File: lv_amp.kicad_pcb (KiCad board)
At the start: 2 copper layers, 127 x 76.2 mm, 87 parts, among them J1 Jack-DC, J2 AudioJack2, J3 AudioJack2, Q1 Q_NMOS_DGS, U1 MAX1771xSA, U2 TL072, U3 ECC83, U4 ECC83, U5 ECC83

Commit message: alpha1 complete
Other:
- board text added: "lv-amp alpha1"
- board text removed: "lv-amp alpha0"
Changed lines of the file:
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@@
   (gr_line (start 38.1 63.5) (end 38.1 139.7) (layer "Edge.Cuts") (width 0.1))
   (gr_line (start 165.1 139.7) (end 165.1 63.5) (layer "Edge.Cuts") (width 0.1))
-  (gr_text "lv-amp alpha0" (at 140 80) (layer "B.SilkS")
+  (gr_text "lv-amp alpha1" (at 140 80) (layer "B.SilkS")
     (effects (font (size 1 1) (thickness 0.15)) (justify mirror))
   )

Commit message: shuffle stuff around to minimize antenna length
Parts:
- moved C6 11.9 mm to (129.0, 92.2), turned to 0 degrees
- moved C4 6.82 mm to (118.5, 97.2), turned to -90 degrees
- moved R7 4.37 mm to (120.0, 89.2), turned to -90 degrees
- moved C5 3.18 mm to (113.5, 87.5)
- moved C7 2.38 mm to (122.8, 98.5), turned to 0 degrees
- moved R11 2.36 mm to (135.0, 91.8), turned to -90 degrees
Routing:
- net +12V: track 223.4 -> 232.8 mm
- net /u1ap: track 31.1 -> 32.8 mm, vias 0 -> 1
- net /q1s: track 15.3 -> 16.6 mm
- net Net-(R7-Pad1): track 7.02 -> 5.81 mm
- net HT: track 201.4 -> 200.3 mm
- net GND: vias 11 -> 12

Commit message: 5v zener
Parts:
- D2: value Zener 3.3V -> Zener 5V
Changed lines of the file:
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@@
   (net 35 "Net-(R7-Pad1)")
   (net 36 "Net-(R6-Pad1)")
-  (net 37 "Net-(R21-Pad2)")
+  (net 37 "Net-(C24-Pad1)")
   (net 38 "/u3ag")
   (net 39 "Net-(R24-Pad1)")
@@
       (effects (font (size 1 1) (thickness 0.15)))
     )
-    (fp_text value "Zener 3.3V" (at 0 2.5) (layer "F.Fab")
+    (fp_text value "Zener 5V" (at 0 2.5) (layer "F.Fab")
       (effects (font (size 1 1) (thickness 0.15)))
     )
@@
     (pad "" smd rect locked (at -1 0.95 180) (size 0.9 0.8) (layers "F.Cu" "F.Paste" "F.Mask"))
     (pad "1" smd rect locked (at 1 0 180) (size 0.9 0.8) (layers "F.Cu" "F.Paste" "F.Mask")
-      (net 37 "Net-(R21-Pad2)") (pinfunction "K") (pintype "passive"))
+      (net 37 "Net-(C24-Pad1)") (pinfunction "K") (pintype "passive"))
     (pad "2" smd rect locked (at -1 -0.95 180) (size 0.9 0.8) (layers "F.Cu" "F.Paste" "F.Mask")
       (net 9 "GND") (pinfunction "A") (pintype "passive"))
@@
     (fp_circle (center 0 0) (end 2 0) (layer "F.Fab") (width 0.1) (fill none))
     (pad "1" smd roundrect locked (at -1.8 0) (size 2.6 1.6) (layers "F.Cu" "F.Paste" "F.Mask") (roundrect_rratio 0.15625)
-      (net 37 "Net-(R21-Pad2)") (pintype "passive"))
+      (net 37 "Net-(C24-Pad1)") (pintype "passive"))
     (pad "2" smd roundrect locked (at 1.8 0) (size 2.6 1.6) (layers "F.Cu" "F.Paste" "F.Mask") (roundrect_rratio 0.15625)
       (net 9 "GND") (pintype "passive"))
@@
       (net 9 "GND") (pinfunction "V-") (pintype "power_in"))
     (pad "5" smd roundrect locked (at 2.575 1.905 90) (size 1.75 0.6) (layers "F.Cu" "F.Paste" "F.Mask") (roundrect_rratio 0.25)
-      (net 37 "Net-(R21-Pad2)") (pinfunction "+") (pintype "input"))
+      (net 37 "Net-(C24-Pad1)") (pinfunction "+") (pintype "input"))
     (pad "6" smd roundrect locked (at 2.575 0.635 90) (size 1.75 0.6) (layers "F.Cu" "F.Paste" "F.Mask") (roundrect_rratio 0.25)
       (net 49 "Net-(U2-Pad3)") (pinfunction "-") (pintype "input"))
@@
       (net 17 "+12V") (pintype "passive"))
     (pad "2" smd roundrect locked (at 0.825 0) (size 0.8 0.95) (layers "F.Cu" "F.Paste" "F.Mask") (roundrect_rratio 0.25)
-      (net 37 "Net-(R21-Pad2)") (pintype "passive"))
+      (net 37 "Net-(C24-Pad1)") (pintype "passive"))
     (model "${KICAD6_3DMODEL_DIR}/Resistor_SMD.3dshapes/R_0603_1608Metric.wrl"
       (offset (xyz 0 0 0))

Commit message: use 5.1 zener
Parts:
- D2: value Zener 5V -> Zener 5.1V
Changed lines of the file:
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@@
       (effects (font (size 1 1) (thickness 0.15)))
     )
-    (fp_text value "Zener 5V" (at 0 2.5) (layer "F.Fab")
+    (fp_text value "Zener 5.1V" (at 0 2.5) (layer "F.Fab")
       (effects (font (size 1 1) (thickness 0.15)))
     )

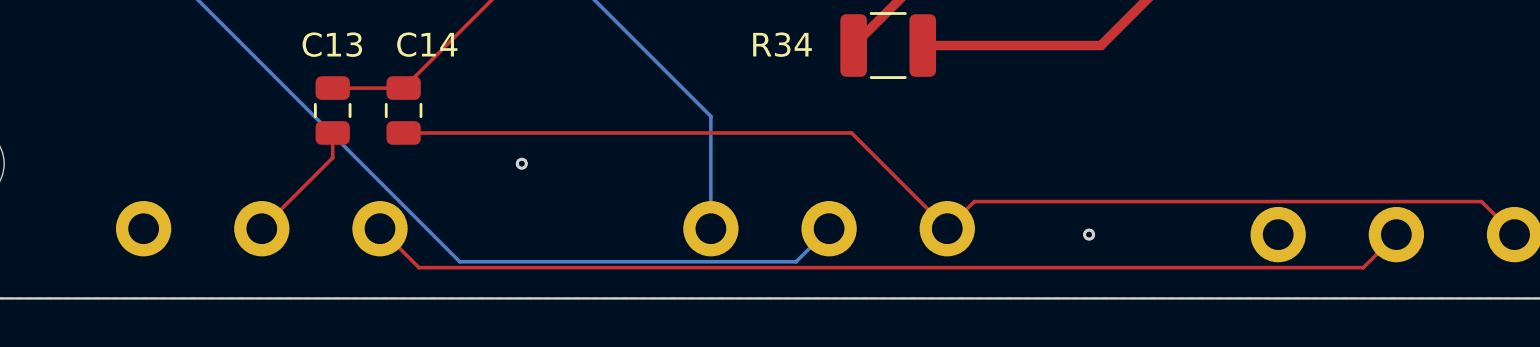
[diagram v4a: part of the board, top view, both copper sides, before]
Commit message: Oops un-flip mid pot
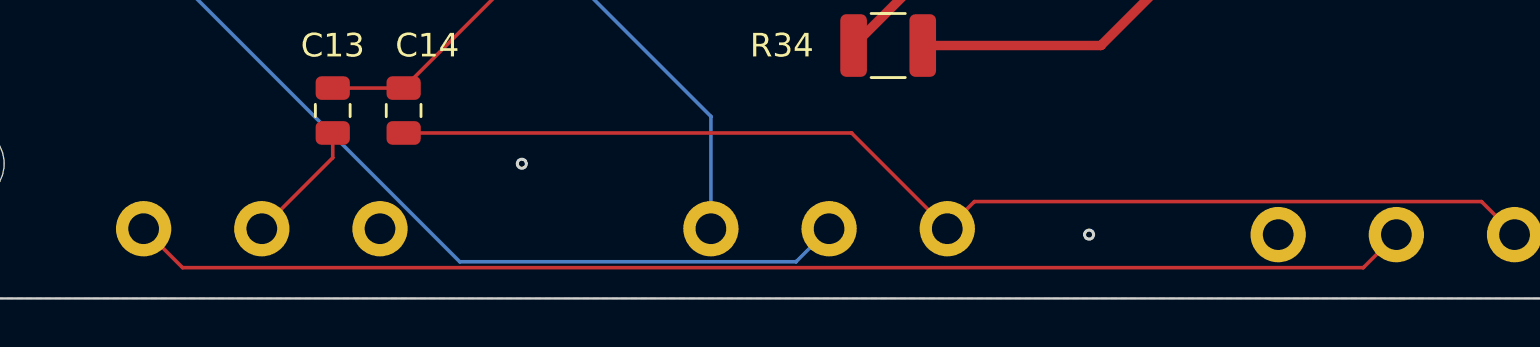
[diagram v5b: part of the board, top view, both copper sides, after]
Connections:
- RV4 pad 1: Net-(RV2-Pad2) -> GND
- RV4 pad 3: GND -> Net-(RV2-Pad2)
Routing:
- net Net-(RV2-Pad2): track 44.3 -> 54.3 mm
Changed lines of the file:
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@@
     (property "Sheetfile" "lv_amp.kicad_sch")
     (property "Sheetname" "")
-    (property "Source" "https://www.tubesandmore.com/products/socket-9-pin-ceramic-pc-mount-bottom-or-pc-mount")
+    (property "Vendor" "https://www.tubesandmore.com/products/socket-9-pin-ceramic-pc-mount-bottom-or-pc-mount")
     (fp_text reference "U3" (at 4 15) (layer "B.SilkS")
       (effects (font (size 1 1) (thickness 0.15)) (justify mirror))
@@
     (property "Sheetfile" "lv_amp.kicad_sch")
     (property "Sheetname" "")
-    (property "source" "https://www.tubesandmore.com/products/potentiometer-alpha-audio-solid-shaft-pc-lead-16mm")
+    (property "Vendor" "https://www.tubesandmore.com/products/potentiometer-alpha-audio-solid-shaft-pc-lead-16mm")
     (attr through_hole)
     (fp_text reference "RV2" (at -5 -1 180) (layer "B.SilkS")
@@
     (property "Sheetfile" "lv_amp.kicad_sch")
     (property "Sheetname" "")
-    (property "Source" "https://www.tubesandmore.com/products/potentiometer-alpha-audio-solid-shaft-pc-lead-16mm")
+    (property "Vendor" "https://www.tubesandmore.com/products/potentiometer-alpha-linear-solid-shaft-pc-lead-16mm")
     (attr through_hole)
     (fp_text reference "RV4" (at -4.75 0 180) (layer "B.SilkS")
@@
     (fp_line (start 1.5 1.5) (end 6.5 1.5) (layer "B.Fab") (width 0.1))
     (pad "1" thru_hole circle locked (at 0 0 270) (size 2.34 2.34) (drill 1.3) (layers *.Cu *.Mask)
-      (net 48 "Net-(RV2-Pad2)") (pinfunction "1") (pintype "passive"))
+      (net 9 "GND") (pinfunction "1") (pintype "passive"))
     (pad "2" thru_hole circle locked (at 0 5 270) (size 2.34 2.34) (drill 1.3) (layers *.Cu *.Mask)
       (net 11 "Net-(C13-Pad2)") (pinfunction "2") (pintype "passive"))
     (pad "3" thru_hole circle locked (at 0 10 270) (size 2.34 2.34) (drill 1.3) (layers *.Cu *.Mask)
-      (net 9 "GND") (pinfunction "3") (pintype "passive"))
+      (net 48 "Net-(RV2-Pad2)") (pinfunction "3") (pintype "passive"))
     (model "${KICAD6_3DMODEL_DIR}/Potentiometer_THT.3dshapes/Potentiometer_Piher_T-16H_Single_Horizontal.wrl"
       (offset (xyz 0 0 0))
@@
     (property "Sheetfile" "lv_amp.kicad_sch")
     (property "Sheetname" "")
+    (property "Vendor" "https://www.tubesandmore.com/products/socket-9-pin-ceramic-pc-mount-bottom-or-pc-mount")
     (fp_text reference "U5" (at -7.1 12.7) (layer "B.SilkS")
       (effects (font (size 1 1) (thickness 0.15)) (justify mirror))
@@
     (property "Sheetfile" "lv_amp.kicad_sch")
     (property "Sheetname" "")
-    (property "Source" "https://www.tubesandmore.com/products/potentiometer-alpha-audio-solid-shaft-pc-lead-16mm")
+    (property "Vendor" "https://www.tubesandmore.com/products/potentiometer-alpha-audio-solid-shaft-pc-lead-16mm")
     (attr through_hole)
     (fp_text reference "RV1" (at -4.75 -1 180) (layer "B.SilkS")
@@
     (property "Sheetfile" "lv_amp.kicad_sch")
     (property "Sheetname" "")
-    (property "Source" "https://www.tubesandmore.com/products/potentiometer-alpha-audio-solid-shaft-pc-lead-16mm")
+    (property "Vendor" "https://www.tubesandmore.com/products/potentiometer-alpha-linear-solid-shaft-pc-lead-16mm")
     (attr through_hole)
     (fp_text reference "RV3" (at -4.75 -1 180) (layer "B.SilkS")
@@
     (property "Sheetfile" "lv_amp.kicad_sch")
     (property "Sheetname" "")
+    (property "Vendor" "https://www.tubesandmore.com/products/potentiometer-alpha-audio-solid-shaft-pc-lead-16mm")
     (attr exclude_from_pos_files)
     (fp_text reference "TP1" (at 0 3) (layer "B.SilkS")
@@
   (segment (start 76.420396 74) (end 71.909831 69.489435) (width 0.4) (layer "F.Cu") (net 46))
   (segment (start 76.9625 74) (end 76.420396 74) (width 0.4) (layer "F.Cu") (net 46))
-  (segment (start 101.601889 138.398111) (end 61.648111 138.398111) (width 0.1524) (layer "F.Cu") (net 48))
-  (segment (start 61.648111 138.398111) (end 60 136.75) (width 0.1524) (layer "F.Cu") (net 48))
-  (segment (start 103 137) (end 101.601889 138.398111) (width 0.1524) (layer "F.Cu") (net 48))
+  (segment (start 50 136.75) (end 51.648111 138.398111) (width 0.1524) (layer "F.Cu") (net 48))
+  (segment (start 101.601889 138.398111) (end 103 137) (width 0.1524) (layer "F.Cu") (net 48))
+  (segment (start 51.648111 138.398111) (end 101.601889 138.398111) (width 0.1524) (layer "F.Cu") (net 48))
   (segment (start 49.765 116.305) (end 49.765 121.455) (width 0.1524) (layer "F.Cu") (net 49))
   (segment (start 48.495 116.305) (end 49.765 116.305) (width 0.1524) (layer "F.Cu") (net 49))

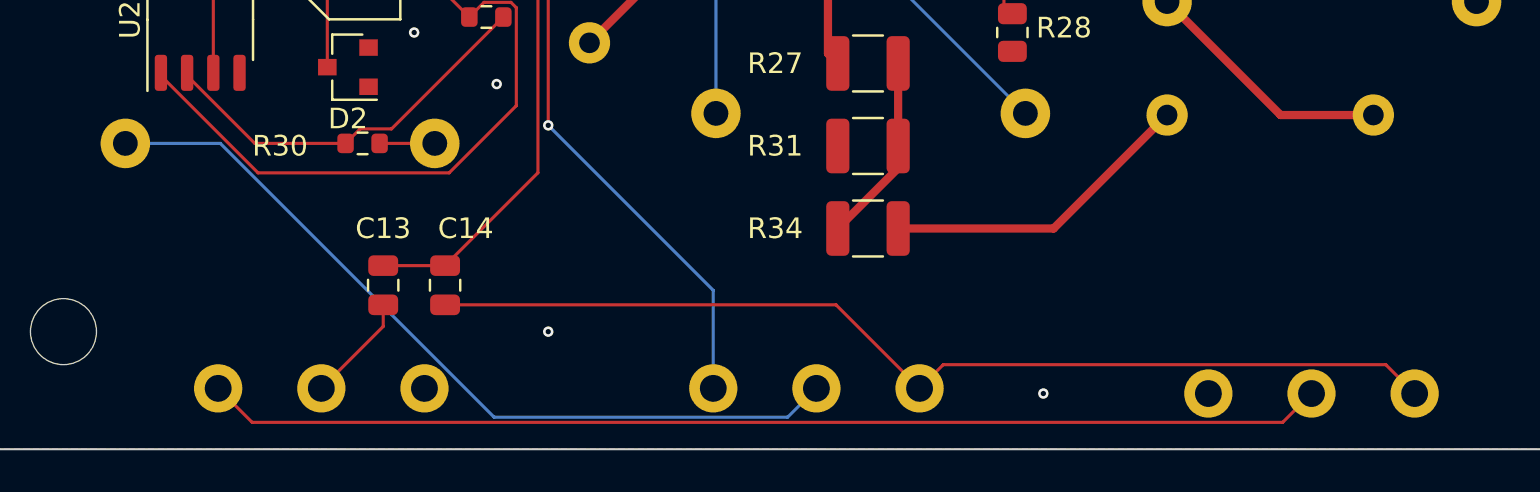
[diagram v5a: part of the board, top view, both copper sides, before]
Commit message: Errata: flip pot order
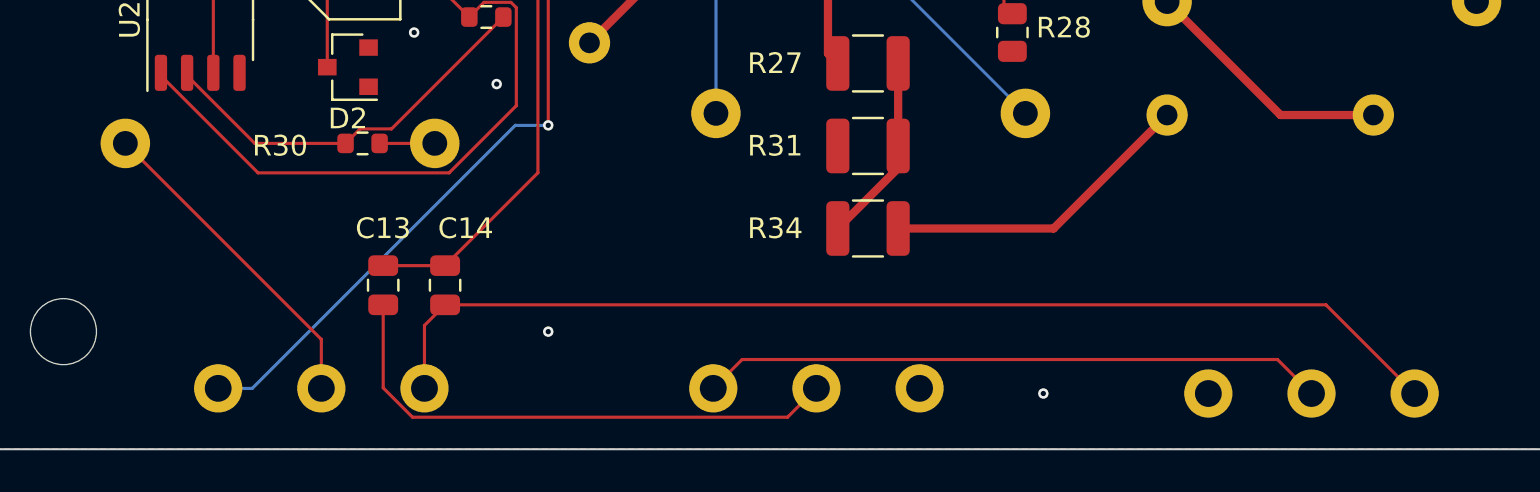
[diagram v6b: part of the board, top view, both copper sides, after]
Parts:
- moved RV3 24.0 mm to (60.0, 136.8)
- moved RV4 24.0 mm to (84.0, 136.8)
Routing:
- net Net-(RV2-Pad2): track 54.3 -> 30.3 mm
- net Net-(C23-Pad1): track 39.6 -> 15.8 mm
- net Net-(C13-Pad2): track 5.29 -> 26.2 mm
- net Net-(C2-Pad2): track 59.1 -> 64.3 mm
- net Net-(C14-Pad2): track 49.7 -> 53.2 mm
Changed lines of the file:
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@@
   )
   (footprint "Potentiometer_THT:Potentiometer_Piher_T-16H_Single_Horizontal" (layer "B.Cu")
-    (at 60 136.75 -90)
+    (at 84 136.75 -90)
     (descr "Potentiometer, horizontal, Piher T-16H Single, http://www.piher-nacesa.com/pdf/22-T16v03.pdf")
     (tags "Potentiometer horizontal Piher T-16H Single")
@@
   )
   (footprint "Potentiometer_THT:Potentiometer_Piher_T-16H_Single_Horizontal" (layer "B.Cu")
-    (at 84 136.75 -90)
+    (at 60 136.75 -90)
     (descr "Potentiometer, horizontal, Piher T-16H Single, http://www.piher-nacesa.com/pdf/22-T16v03.pdf")
     (tags "Potentiometer horizontal Piher T-16H Single")
@@
   (segment (start 57.49376 87.19688) (end 58.29688 88) (width 0.1524) (layer "F.Cu") (net 4))
   (via (at 66 124) (size 0.508) (drill 0.254) (layers "F.Cu" "B.Cu") (net 4))
-  (segment (start 74 132) (end 66 124) (width 0.1524) (layer "B.Cu") (net 4))
-  (segment (start 74 136.75) (end 74 132) (width 0.1524) (layer "B.Cu") (net 4))
+  (segment (start 51.654629 136.75) (end 64.404629 124) (width 0.1524) (layer "B.Cu") (net 4))
+  (segment (start 50 136.75) (end 51.654629 136.75) (width 0.1524) (layer "B.Cu") (net 4))
+  (segment (start 64.404629 124) (end 66 124) (width 0.1524) (layer "B.Cu") (net 4))
   (segment (start 137.2 117.8375) (end 138.0375 117) (width 0.1524) (layer "F.Cu") (net 5))
   (segment (start 138.0375 111.474266) (end 135.010565 108.447331) (width 0.1524) (layer "F.Cu") (net 5))
@@
   (segment (start 125.5 107) (end 125.75 107.25) (width 0.4) (layer "B.Cu") (net 10))
   (segment (start 125.5 101.5375) (end 125.5 107) (width 0.4) (layer "B.Cu") (net 10))
-  (segment (start 55 136.75) (end 58 133.75) (width 0.1524) (layer "F.Cu") (net 11))
-  (segment (start 58 133.75) (end 58 132.7) (width 0.1524) (layer "F.Cu") (net 11))
-  (segment (start 108 137) (end 106.601889 135.601889) (width 0.1524) (layer "F.Cu") (net 12))
-  (segment (start 85.148111 135.601889) (end 84 136.75) (width 0.1524) (layer "F.Cu") (net 12))
-  (segment (start 106.601889 135.601889) (end 85.148111 135.601889) (width 0.1524) (layer "F.Cu") (net 12))
-  (segment (start 84 136.75) (end 79.95 132.7) (width 0.1524) (layer "F.Cu") (net 12))
-  (segment (start 79.95 132.7) (end 61 132.7) (width 0.1524) (layer "F.Cu") (net 12))
+  (segment (start 58 136.727229) (end 59.420882 138.148111) (width 0.1524) (layer "F.Cu") (net 11))
+  (segment (start 58 132.7) (end 58 136.727229) (width 0.1524) (layer "F.Cu") (net 11))
+  (segment (start 59.420882 138.148111) (end 77.601889 138.148111) (width 0.1524) (layer "F.Cu") (net 11))
+  (segment (start 77.601889 138.148111) (end 79 136.75) (width 0.1524) (layer "F.Cu") (net 11))
+  (segment (start 60 136.75) (end 60 133.7) (width 0.1524) (layer "F.Cu") (net 12))
+  (segment (start 103.7 132.7) (end 108 137) (width 0.1524) (layer "F.Cu") (net 12))
+  (segment (start 61 132.7) (end 103.7 132.7) (width 0.1524) (layer "F.Cu") (net 12))
+  (segment (start 60 133.7) (end 61 132.7) (width 0.1524) (layer "F.Cu") (net 12))
   (segment (start 124.9625 133.4375) (end 124.9625 131.5) (width 0.1524) (layer "F.Cu") (net 13))
   (segment (start 124.4 134) (end 124.4 134.15) (width 0.1524) (layer "F.Cu") (net 13))
@@
   (segment (start 78.5375 109) (end 78.5375 108.5375) (width 0.4) (layer "F.Cu") (net 25))
   (segment (start 68 110) (end 68 106.825) (width 0.4) (layer "F.Cu") (net 26))
-  (segment (start 50.102229 124.875) (end 63.37534 138.148111) (width 0.1524) (layer "B.Cu") (net 27))
-  (segment (start 45.5 124.875) (end 50.102229 124.875) (width 0.1524) (layer "B.Cu") (net 27))
-  (segment (start 63.37534 138.148111) (end 77.601889 138.148111) (width 0.1524) (layer "B.Cu") (net 27))
-  (segment (start 77.601889 138.148111) (end 79 136.75) (width 0.1524) (layer "B.Cu") (net 27))
+  (segment (start 55 136.75) (end 55 134.375) (width 0.1524) (layer "F.Cu") (net 27))
+  (segment (start 55 134.375) (end 45.5 124.875) (width 0.1524) (layer "F.Cu") (net 27))
   (segment (start 132 75.625) (end 149.905 75.625) (width 1) (layer "F.Cu") (net 28))
   (segment (start 132 75.625) (end 128.835 72.46) (width 1) (layer "F.Cu") (net 28))
@@
   (segment (start 76.420396 74) (end 71.909831 69.489435) (width 0.4) (layer "F.Cu") (net 46))
   (segment (start 76.9625 74) (end 76.420396 74) (width 0.4) (layer "F.Cu") (net 46))
-  (segment (start 50 136.75) (end 51.648111 138.398111) (width 0.1524) (layer "F.Cu") (net 48))
-  (segment (start 101.601889 138.398111) (end 103 137) (width 0.1524) (layer "F.Cu") (net 48))
-  (segment (start 51.648111 138.398111) (end 101.601889 138.398111) (width 0.1524) (layer "F.Cu") (net 48))
+  (segment (start 75.398111 135.351889) (end 101.351889 135.351889) (width 0.1524) (layer "F.Cu") (net 48))
+  (segment (start 101.351889 135.351889) (end 103 137) (width 0.1524) (layer "F.Cu") (net 48))
+  (segment (start 74 136.75) (end 75.398111 135.351889) (width 0.1524) (layer "F.Cu") (net 48))
   (segment (start 49.765 116.305) (end 49.765 121.455) (width 0.1524) (layer "F.Cu") (net 49))
   (segment (start 48.495 116.305) (end 49.765 116.305) (width 0.1524) (layer "F.Cu") (net 49))

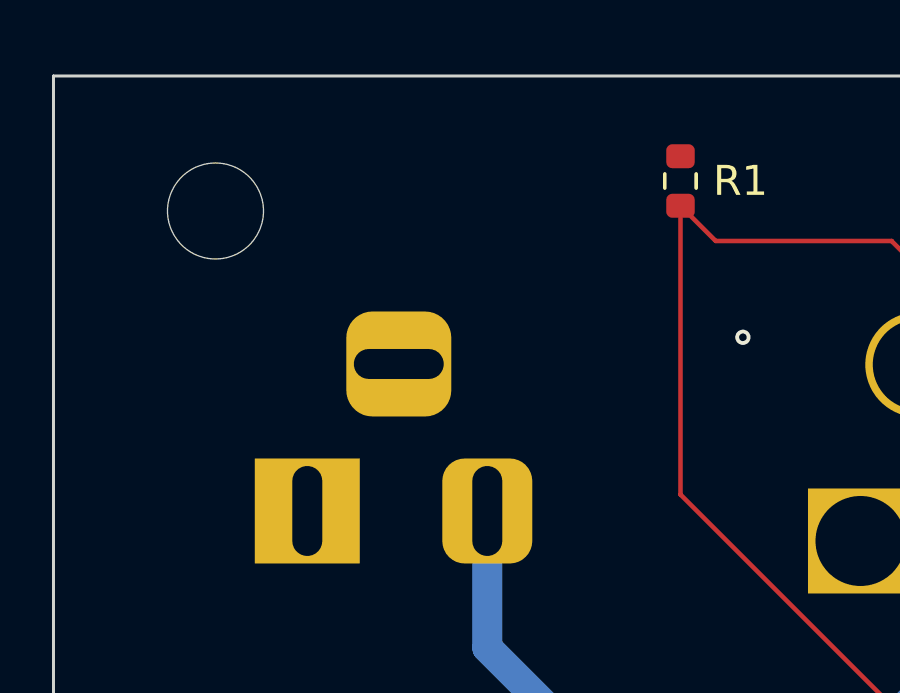
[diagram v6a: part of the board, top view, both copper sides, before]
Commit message: errata - add power switch
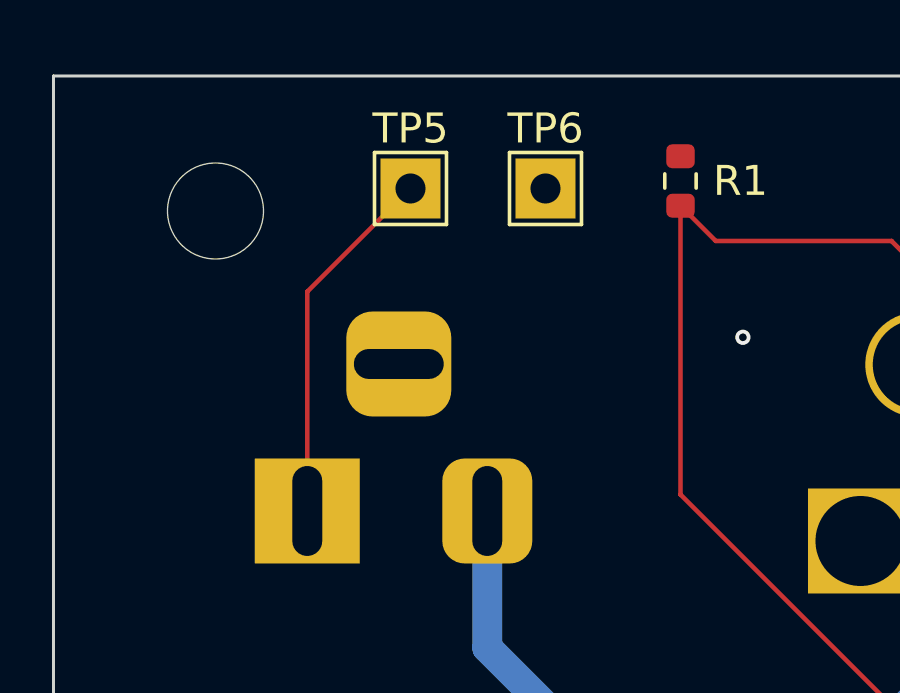
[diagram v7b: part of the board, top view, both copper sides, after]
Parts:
- added TP5: TestPoint, TestPoint:TestPoint_THTPad_2.0x2.0mm_Drill1.0mm, F.Cu at (50.0, 67.2)
- added TP6: TestPoint, TestPoint:TestPoint_THTPad_2.0x2.0mm_Drill1.0mm, F.Cu at (54.5, 67.2)
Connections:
- J1 pad 2: GND -> Net-(J1-Pad2)
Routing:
- net Net-(J1-Pad2): track 0.00 -> 12.2 mm
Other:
- board text added: "lv-amp r1.0"
- board text removed: "lv-amp alpha1"
